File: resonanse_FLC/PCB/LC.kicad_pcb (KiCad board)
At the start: 2 copper layers, 93 x 25 mm, 39 parts, among them J1 Conn_01x02, J2 Conn_01x02, J3 Conn_01x02, J4 Conn_01x02, J5 RF, Q1 BFT92, Q2 BFT92, Q3 BC857, Q4 BF998, Q5 SS9018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

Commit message: finish PCB
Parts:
- C10, C12, C14, C4, J5, U1: moved to B.Cu
- J3, J4: footprint lc_probe:SolderWirePad_double_SMD_2x5mm -> Pin_Headers:Pin_Header_Straight_1x02_Pitch2.54mm; moved to B.Cu
- L1: footprint lc_probe:Choke_Toroid_horizontal_Diameter10-5mm_Amidon-T37_2 -> Choke_Toroid_ThroughHole:Choke_Toroid_6,5x13mm_Vertical
- moved C14 55.4 mm to (181.5, 60.5), turned to 270 degrees
- moved U1 53.2 mm to (172.5, 57.5)
- moved C13 51.6 mm to (177.6, 62.4), turned to 270 degrees
- moved D1 20.6 mm to (150.0, 71.8)
- moved C3 19.4 mm to (140.5, 72.5)
- moved R3 19.4 mm to (143.0, 70.0)
- moved C2 19.3 mm to (138.0, 70.0)
- moved C9 18.5 mm to (170.0, 71.0), turned to 180 degrees
- moved R9 18.2 mm to (165.5, 65.5)
- moved R8 17.9 mm to (165.5, 68.0)
- moved R1 17.9 mm to (136.2, 62.6), turned to 270 degrees
- moved Q5 17.8 mm to (165.5, 71.0)
- moved Q4 17.3 mm to (156.0, 71.0)
- moved C11 17.1 mm to (172.5, 62.4)
- moved C10 17.1 mm to (159.0, 60.5), turned to 270 degrees
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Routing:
- net GND: track 0.00 -> 337.2 mm, vias 0 -> 77
- net Net-(C10-Pad1): track 0.00 -> 60.7 mm
- net Net-(C2-Pad2): track 10.7 -> 50.2 mm
- net Net-(C9-Pad1): track 0.00 -> 35.2 mm
- net Net-(C6-Pad2): track 0.00 -> 18.8 mm
- net Net-(C3-Pad1): track 0.00 -> 18.3 mm
- net Net-(C5-Pad1): track 0.00 -> 18.1 mm
- net Net-(C4-Pad2): track 0.00 -> 13.1 mm
- net Net-(C6-Pad1): track 0.00 -> 11.4 mm
- net Net-(C11-Pad1): track 0.00 -> 11.2 mm
- net Net-(C13-Pad1): track 0.00 -> 11.2 mm
- net Net-(C9-Pad2): track 0.00 -> 11.1 mm
- net Net-(Q1-Pad2): track 0.00 -> 7.30 mm
- net Net-(C7-Pad1): track 0.00 -> 6.30 mm
- net Net-(Q3-Pad3): track 0.00 -> 6.00 mm
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- added copper zone on B.Cu, net GND
- added copper zone on F.Cu, net GND
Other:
- board size 93 x 25 mm -> 91.5 x 22.5 mm
- net class Default: trace_width 0.25 -> 0.4

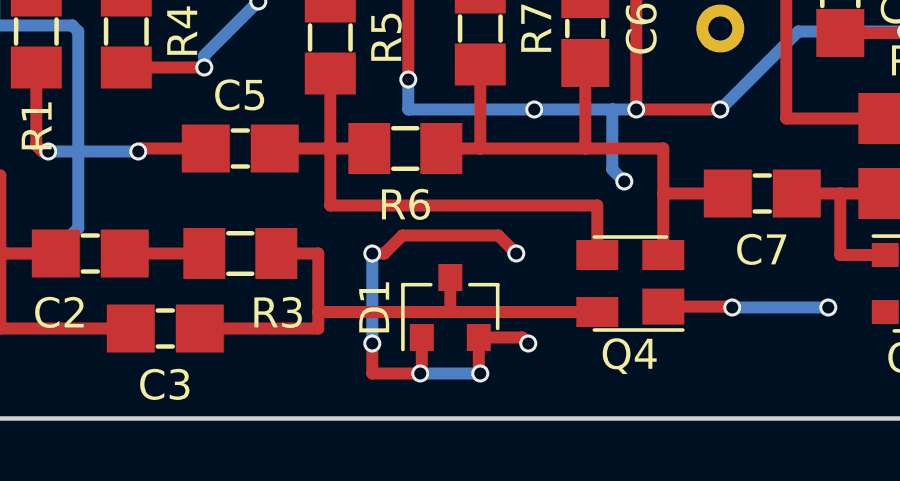
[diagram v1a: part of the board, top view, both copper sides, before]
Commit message: fix PCB VIA near D1
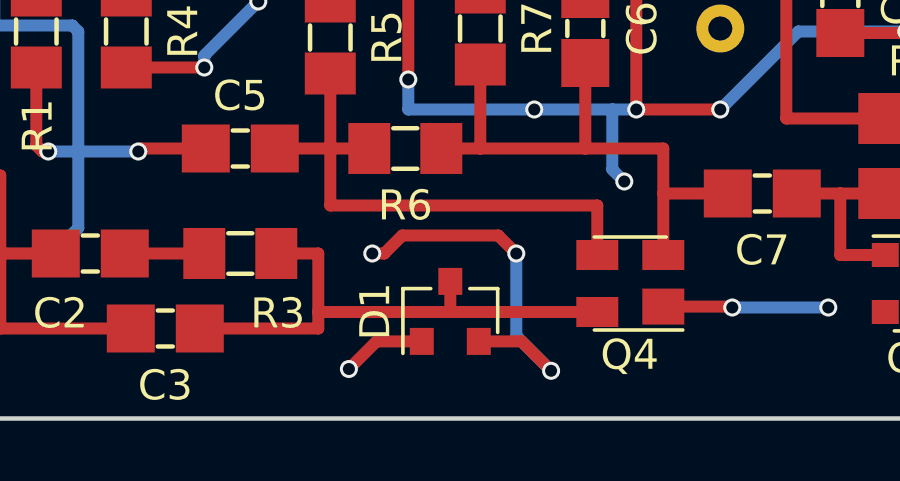
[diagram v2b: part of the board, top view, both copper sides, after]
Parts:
- moved D1 0.13 mm to (150.0, 71.9)
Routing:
- net GND: track 337.2 -> 335.4 mm, vias 77 -> 75
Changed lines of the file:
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@@
     (thickness 1.6)
     (drawings 14)
-    (tracks 324)
+    (tracks 318)
     (zones 0)
     (modules 39)
@@
   )
   (module TO_SOT_Packages_SMD:SOT-23 (layer F.Cu)
-    (at 150 71.8 90)
+    (at 150 71.93 90)
     (descr "SOT-23, Standard")
     (tags SOT-23)
@@
   (gr_line (start 194.5 58) (end 196 56.5) (angle 90) (layer Edge.Cuts) (width 0.15))
   (gr_line (start 194.5 72) (end 194.5 58) (angle 90) (layer Edge.Cuts) (width 0.15))
+  (segment (start 152.2 70) (end 152.2 72.75) (width 0.4) (layer B.Cu) (net 1))
+  (segment (start 152.38 72.93) (end 153.36 73.91) (width 0.4) (layer F.Cu) (net 1))
+  (via (at 153.36 73.91) (size 0.6) (drill 0.4) (layers F.Cu B.Cu) (net 1))
+  (segment (start 150.95 72.93) (end 152.38 72.93) (width 0.4) (layer F.Cu) (net 1))
+  (via (at 147.4 70) (size 0.6) (drill 0.4) (layers F.Cu B.Cu) (net 1))
+  (via (at 152.2 70) (size 0.6) (drill 0.4) (layers F.Cu B.Cu) (net 1))
+  (segment (start 151.6 69.4) (end 152.2 70) (width 0.4) (layer F.Cu) (net 1))
+  (segment (start 148.4 69.4) (end 151.6 69.4) (width 0.4) (layer F.Cu) (net 1))
+  (segment (start 147.8 70) (end 148.4 69.4) (width 0.4) (layer F.Cu) (net 1))
+  (segment (start 147.4 70) (end 147.8 70) (width 0.4) (layer F.Cu) (net 1))
+  (segment (start 152.2 72.75) (end 153.36 73.91) (width 0.4) (layer B.Cu) (net 1))
+  (segment (start 149.05 72.93) (end 147.54 72.93) (width 0.4) (layer F.Cu) (net 1))
+  (via (at 146.62 73.85) (size 0.6) (drill 0.4) (layers F.Cu B.Cu) (net 1))
+  (segment (start 147.54 72.93) (end 146.62 73.85) (width 0.4) (layer F.Cu) (net 1))
   (segment (start 183.5 54.5) (end 193.25 54.5) (width 0.4) (layer B.Cu) (net 1))
   (via (at 193.25 54.5) (size 0.6) (drill 0.4) (layers F.Cu B.Cu) (net 1))
@@
   (segment (start 181.25 66) (end 177.5 66) (width 0.4) (layer B.Cu) (net 1))
   (via (at 190.25 73.25) (size 0.6) (drill 0.4) (layers F.Cu B.Cu) (net 1))
-  (segment (start 191.65 61.38) (end 185.87 61.38) (width 0.4) (layer B.Cu) (net 1) (status 400000))
+  (segment (start 191.65 61.38) (end 185.87 61.38) (width 0.4) (layer B.Cu) (net 1))
   (segment (start 171.25 54.75) (end 165.25 54.75) (width 0.4) (layer F.Cu) (net 1))
   (segment (start 171.5 54.5) (end 171.25 54.75) (width 0.4) (layer F.Cu) (net 1))
@@
   (segment (start 172.5 66) (end 172.5 68.75) (width 0.4) (layer B.Cu) (net 1))
   (via (at 172.5 68.75) (size 0.6) (drill 0.4) (layers F.Cu B.Cu) (net 1))
-  (segment (start 177.58 63.55) (end 175.05 63.55) (width 0.4) (layer F.Cu) (net 1) (status 400000))
+  (segment (start 177.58 63.55) (end 175.05 63.55) (width 0.4) (layer F.Cu) (net 1))
   (via (at 175 63.5) (size 0.6) (drill 0.4) (layers F.Cu B.Cu) (net 1))
   (segment (start 175.05 63.55) (end 175 63.5) (width 0.4) (layer F.Cu) (net 1))
   (via (at 172.5 66) (size 0.6) (drill 0.4) (layers F.Cu B.Cu) (net 1))
-  (segment (start 172.5 63.55) (end 172.5 66) (width 0.4) (layer F.Cu) (net 1) (status 400000))
-  (segment (start 177.58 65.92) (end 177.58 63.55) (width 0.4) (layer F.Cu) (net 1) (status 800000))
+  (segment (start 172.5 63.55) (end 172.5 66) (width 0.4) (layer F.Cu) (net 1))
+  (segment (start 177.58 65.92) (end 177.58 63.55) (width 0.4) (layer F.Cu) (net 1))
   (segment (start 177.5 66) (end 177.58 65.92) (width 0.4) (layer F.Cu) (net 1))
   (via (at 177.5 66) (size 0.6) (drill 0.4) (layers F.Cu B.Cu) (net 1))
@@
   (via (at 108.25 60.25) (size 0.6) (drill 0.4) (layers F.Cu B.Cu) (net 1))
   (segment (start 109 59.5) (end 108.25 60.25) (width 0.4) (layer B.Cu) (net 1))
-  (segment (start 107.25 65.54) (end 107.25 67.5) (width 0.4) (layer F.Cu) (net 1) (status 400000))
+  (segment (start 107.25 65.54) (end 107.25 67.5) (width 0.4) (layer F.Cu) (net 1))
   (via (at 109 68.5) (size 0.6) (drill 0.4) (layers F.Cu B.Cu) (net 1))
   (segment (start 108.25 68.5) (end 109 68.5) (width 0.4) (layer F.Cu) (net 1))
@@
   (segment (start 136.2 66.4) (end 136.2 63.8) (width 0.4) (layer F.Cu) (net 1))
   (segment (start 136.4 66.6) (end 136.2 66.4) (width 0.4) (layer F.Cu) (net 1))
-  (segment (start 147.4 70) (end 147.8 70) (width 0.4) (layer F.Cu) (net 1))
-  (via (at 147.4 70) (size 0.6) (drill 0.4) (layers F.Cu B.Cu) (net 1))
-  (segment (start 147.4 74) (end 147.4 73) (width 0.4) (layer F.Cu) (net 1))
-  (segment (start 149.05 74) (end 147.4 74) (width 0.4) (layer F.Cu) (net 1))
-  (via (at 147.4 73) (size 0.6) (drill 0.4) (layers F.Cu B.Cu) (net 1))
-  (segment (start 147.4 70) (end 147.4 73) (width 0.4) (layer B.Cu) (net 1))
-  (via (at 152.2 70) (size 0.6) (drill 0.4) (layers F.Cu B.Cu) (net 1))
-  (segment (start 151.6 69.4) (end 152.2 70) (width 0.4) (layer F.Cu) (net 1))
-  (segment (start 148.4 69.4) (end 151.6 69.4) (width 0.4) (layer F.Cu) (net 1))
-  (segment (start 147.8 70) (end 148.4 69.4) (width 0.4) (layer F.Cu) (net 1))
-  (segment (start 150.95 72.8) (end 152.4 72.8) (width 0.4) (layer F.Cu) (net 1))
-  (via (at 152.6 73) (size 0.6) (drill 0.4) (layers F.Cu B.Cu) (net 1))
-  (segment (start 152.4 72.8) (end 152.6 73) (width 0.4) (layer F.Cu) (net 1))
-  (segment (start 150.95 72.8) (end 150.95 73.95) (width 0.4) (layer F.Cu) (net 1))
-  (segment (start 149 74) (end 149.05 74) (width 0.4) (layer F.Cu) (net 1))
-  (via (at 149 74) (size 0.6) (drill 0.4) (layers F.Cu B.Cu) (net 1))
-  (segment (start 151 74) (end 149 74) (width 0.4) (layer B.Cu) (net 1))
-  (via (at 151 74) (size 0.6) (drill 0.4) (layers F.Cu B.Cu) (net 1))
-  (segment (start 150.95 73.95) (end 151 74) (width 0.4) (layer F.Cu) (net 1))
-  (segment (start 149.05 72.8) (end 149.05 74) (width 0.4) (layer F.Cu) (net 1))
   (segment (start 141.8 63.8) (end 141.8 63.4) (width 0.4) (layer B.Cu) (net 1))
   (via (at 141.8 63.8) (size 0.6) (drill 0.4) (layers F.Cu B.Cu) (net 1))
@@
   (segment (start 127.45 66) (end 127.45 67.4) (width 0.4) (layer F.Cu) (net 3))
   (segment (start 139.15 70) (end 141.8 70) (width 0.4) (layer F.Cu) (net 4))
-  (segment (start 150 70.8) (end 150 71.95) (width 0.4) (layer F.Cu) (net 5) (status 10))
+  (segment (start 150 70.93) (end 150 71.95) (width 0.4) (layer F.Cu) (net 5))
   (segment (start 154.9 71.95) (end 150 71.95) (width 0.4) (layer F.Cu) (net 5))
   (segment (start 150 71.95) (end 145.6 71.95) (width 0.4) (layer F.Cu) (net 5))
@@
   (segment (start 166.5 71) (end 167.6 71) (width 0.4) (layer F.Cu) (net 12))
   (segment (start 167.6 71) (end 168.85 71) (width 0.4) (layer F.Cu) (net 12))
-  (segment (start 190.143 65) (end 188 65) (width 0.4) (layer F.Cu) (net 13) (status 400000))
+  (segment (start 190.143 65) (end 188 65) (width 0.4) (layer F.Cu) (net 13))
   (segment (start 185.4 71) (end 185.4 65) (width 0.4) (layer F.Cu) (net 13))
   (segment (start 188 65) (end 185.4 65) (width 0.4) (layer F.Cu) (net 13))
